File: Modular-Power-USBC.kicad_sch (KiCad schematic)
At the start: 17 parts, among them J1 USB_C_Receptacle_PowerOnly_6P, J2 +12v Rail, J3 -12V Rail, U1 LM66100DCK

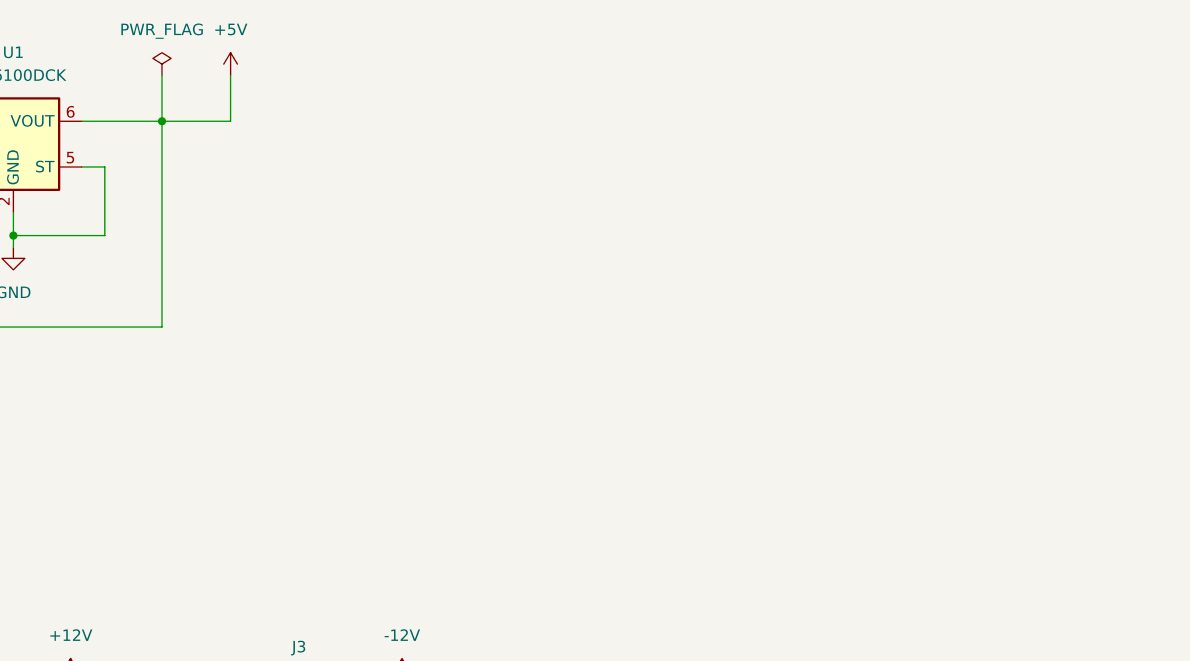
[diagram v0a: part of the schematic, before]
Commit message: Add switch
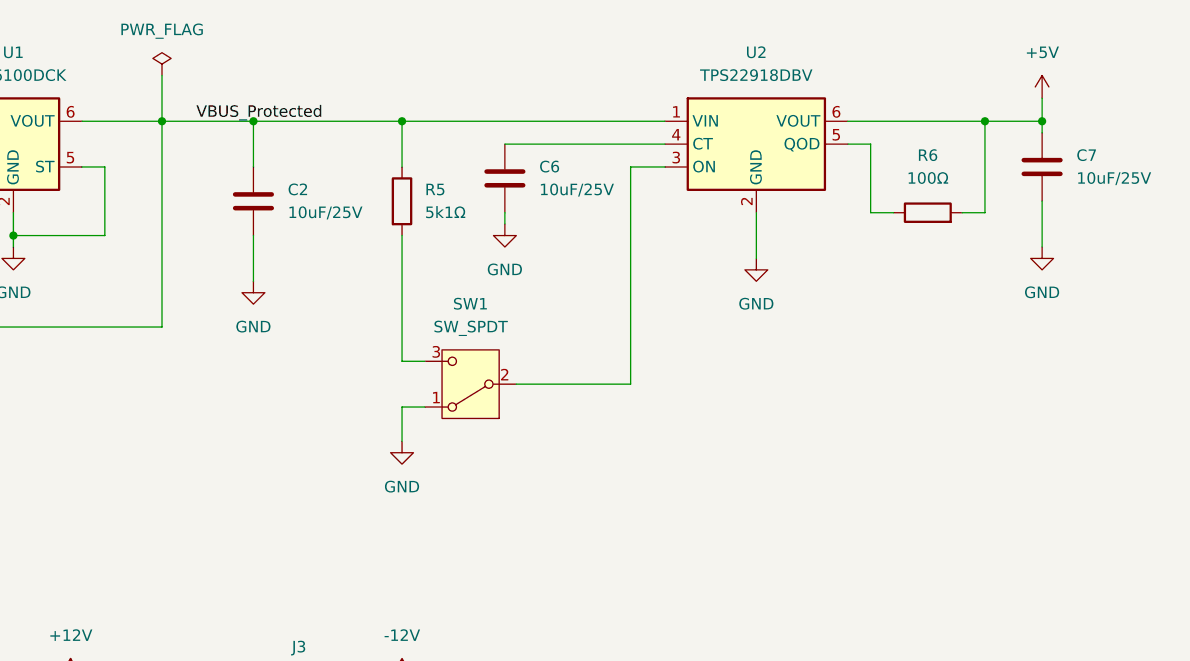
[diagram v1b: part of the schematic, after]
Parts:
- added C2, C6, C7: 10uF/25V, Capacitor_SMD:C_0805_2012Metric_Pad1.18x1.45mm_HandSolder, symbol Device:C
- added R5: 5k1Ω, Resistor_SMD:R_0805_2012Metric_Pad1.20x1.40mm_HandSolder, symbol Device:R
- added R6: 100Ω, Resistor_SMD:R_0805_2012Metric_Pad1.20x1.40mm_HandSolder, symbol Device:R
- added SW1: SW_SPDT, Button_Switch_THT:SW_Slide_SPDT_Straight_CK_OS102011MS2Q, symbol Switch:SW_SPDT
- added U2: TPS22918DBV, Package_TO_SOT_SMD:SOT-23-6, symbol ModularPower:TPS22918DBV
- FB1: footprint (none) -> Modular-Power-USBC:FerriteBead_0805_2012Metric_Pad1.20x1.40mm_HandSolder
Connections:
- net +5V: now also C7.1, R6.2, U2.6 (VOUT); no longer U1.3 (~{CE}), U1.6 (VOUT)
- net GND: now also C2.2, C6.2, C7.2, SW1.1 (A), U2.2 (GND)
- new net: SW1.2 (B), U2.3 (ON)
- new net: R5.2, SW1.3 (C)
- new net: C6.1, U2.4 (CT)
- new net: R6.1, U2.5 (QOD)
- new net VBUS_Protected: C2.1, R5.1, U1.3 (~{CE}), U1.6 (VOUT), U2.1 (VIN)

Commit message: Add README and fixup traces and symbols
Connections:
- net GND: now also J1.SH (SHIELD); no longer J1.S1 (SHIELD)
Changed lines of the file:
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@@
 		(pin "A12"
 		)
-		(pin "S1"
+		(pin "SH"
 		)
 		(instances

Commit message: Drop redundant cap
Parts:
- removed C7: 10uF/25V, Capacitor_SMD:C_0805_2012Metric_Pad1.18x1.45mm_HandSolder, symbol Device:C
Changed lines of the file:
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@@
-	)
-	(junction
-		(at 257.81 43.18)
-		(diameter 0)
-		(color 0 0 0 0)
 	)
 	(junction
@@
 	(wire
 		(pts
-			(xy 257.81 43.18) (xy 257.81 44.45)
-		)
-		(stroke
-			(width 0)
-			(type default)
-		)
-	)
-	(wire
-		(pts
 			(xy 107.95 114.3) (xy 107.95 119.38)
 		)
@@
 	(wire
 		(pts
-			(xy 257.81 52.07) (xy 257.81 57.15)
-		)
-		(stroke
-			(width 0)
-			(type default)
-		)
-	)
-	(wire
-		(pts
 			(xy 198.12 45.72) (xy 215.9 45.72)
 		)
@@
 	(wire
 		(pts
-			(xy 251.46 43.18) (xy 257.81 43.18)
-		)
-		(stroke
-			(width 0)
-			(type default)
-		)
-	)
-	(wire
-		(pts
 			(xy 44.45 120.65) (xy 44.45 118.11)
 		)
@@
 	(wire
 		(pts
-			(xy 257.81 40.64) (xy 257.81 43.18)
+			(xy 251.46 40.64) (xy 251.46 43.18)
 		)
 		(stroke
@@
 	(symbol
 		(lib_id "power:+5V")
-		(at 257.81 40.64 0)
+		(at 251.46 40.64 0)
 		(unit 1)
 		(body_style 1)
@@
 		(fields_autoplaced yes)
 		(property "Reference" "#PWR020"
-			(at 257.81 44.45 0)
+			(at 251.46 44.45 0)
 			(hide yes)
 			(show_name no)
@@
 		)
 		(property "Value" "+5V"
-			(at 257.81 35.56 0)
+			(at 251.46 35.56 0)
 			(show_name no)
 			(do_not_autoplace no)
@@
 		)
 		(property "Footprint" ""
-			(at 257.81 40.64 0)
+			(at 251.46 40.64 0)
 			(hide yes)
 			(show_name no)
@@
 		)
 		(property "Datasheet" ""
-			(at 257.81 40.64 0)
+			(at 251.46 40.64 0)
 			(hide yes)
 			(show_name no)
@@
 		)
 		(property "Description" "Power symbol creates a global label with name \"+5V\""
-			(at 257.81 40.64 0)
+			(at 251.46 40.64 0)
 			(hide yes)
 			(show_name no)
@@
 	)
 	(symbol
-		(lib_id "Device:C")
-		(at 257.81 48.26 0)
-		(unit 1)
-		(body_style 1)
-		(exclude_from_sim no)
-		(in_bom yes)
-		(on_board yes)
-		(in_pos_files yes)
-		(dnp no)
-		(fields_autoplaced yes)
-		(property "Reference" "C7"
-			(at 261.62 46.9899 0)
-			(show_name no)
-			(do_not_autoplace no)
-			(effects
-				(font
-					(size 1.27 1.27)
-				)
-				(justify left)
-			)
-		)
-		(property "Value" "10uF/25V"
-			(at 261.62 49.5299 0)
-			(show_name no)
-			(do_not_autoplace no)
-			(effects
-				(font
-					(size 1.27 1.27)
-				)
-				(justify left)
-			)
-		)
-		(property "Footprint" "Capacitor_SMD:C_0805_2012Metric_Pad1.18x1.45mm_HandSolder"
-			(at 258.7752 52.07 0)
-			(hide yes)
-			(show_name no)
-			(do_not_autoplace no)
-			(effects
-				(font
-					(size 1.27 1.27)
-				)
-			)
-		)
-		(property "Datasheet" ""
-			(at 257.81 48.26 0)
-			(hide yes)
-			(show_name no)
-			(do_not_autoplace no)
-			(effects
-				(font
-					(size 1.27 1.27)
-				)
-			)
-		)
-		(property "Description" "Unpolarized capacitor"
-			(at 257.81 48.26 0)
-			(hide yes)
-			(show_name no)
-			(do_not_autoplace no)
-			(effects
-				(font
-					(size 1.27 1.27)
-				)
-			)
-		)
-		(property "LCSC" "C6119887"
-			(at 257.81 48.26 0)
-			(hide yes)
-			(show_name no)
-			(do_not_autoplace no)
-			(effects
-				(font
-					(size 1.27 1.27)
-				)
-			)
-		)
-		(pin "2"
-		)
-		(pin "1"
-		)
-		(instances
-			(project "Modular-Power-USBC"
-				(path "/f2dd20e6-6351-4f8b-97a2-d33eb2b95f73"
-					(reference "C7")
-					(unit 1)
-				)
-			)
-		)
-	)
-	(symbol
 		(lib_id "Device:R")
 		(at 114.3 157.48 0)
@@
 					(unit 1)
 				)
-			)
-		)
-	)
-	(symbol
-		(lib_id "power:GND")
-		(at 257.81 57.15 0)
-		(unit 1)
-		(body_style 1)
-		(exclude_from_sim no)
-		(in_bom yes)
-		(on_board yes)
-		(in_pos_files yes)
-		(dnp no)
-		(fields_autoplaced yes)
-		(property "Reference" "#PWR019"
-			(at 257.81 63.5 0)
-			(hide yes)
-			(show_name no)
-			(do_not_autoplace no)
-			(effects
-				(font
-					(size 1.27 1.27)
-				)
-			)
-		)
-		(property "Value" "GND"
-			(at 257.81 62.23 0)
-			(show_name no)
-			(do_not_autoplace no)
-			(effects
-				(font
-					(size 1.27 1.27)
-				)
-			)
-		)
-		(property "Footprint" ""
-			(at 257.81 57.15 0)
-			(hide yes)
-			(show_name no)
-			(do_not_autoplace no)
-			(effects
-				(font
-					(size 1.27 1.27)
-				)
-			)
-		)
-		(property "Datasheet" ""
-			(at 257.81 57.15 0)
-			(hide yes)
-			(show_name no)
-			(do_not_autoplace no)
-			(effects
-				(font
-					(size 1.27 1.27)
-				)
-			)
-		)
-		(property "Description" "Power symbol creates a global label with name \"GND\" , ground"
-			(at 257.81 57.15 0)
-			(hide yes)
-			(show_name no)
-			(do_not_autoplace no)
-			(effects
-				(font
-					(size 1.27 1.27)
-				)
-			)
-		)
-		(pin "1"
-		)
-		(instances
-			(project "Modular-Power-USBC"
-				(path "/f2dd20e6-6351-4f8b-97a2-d33eb2b95f73"
-					(reference "#PWR019")
-					(unit 1)
-				)

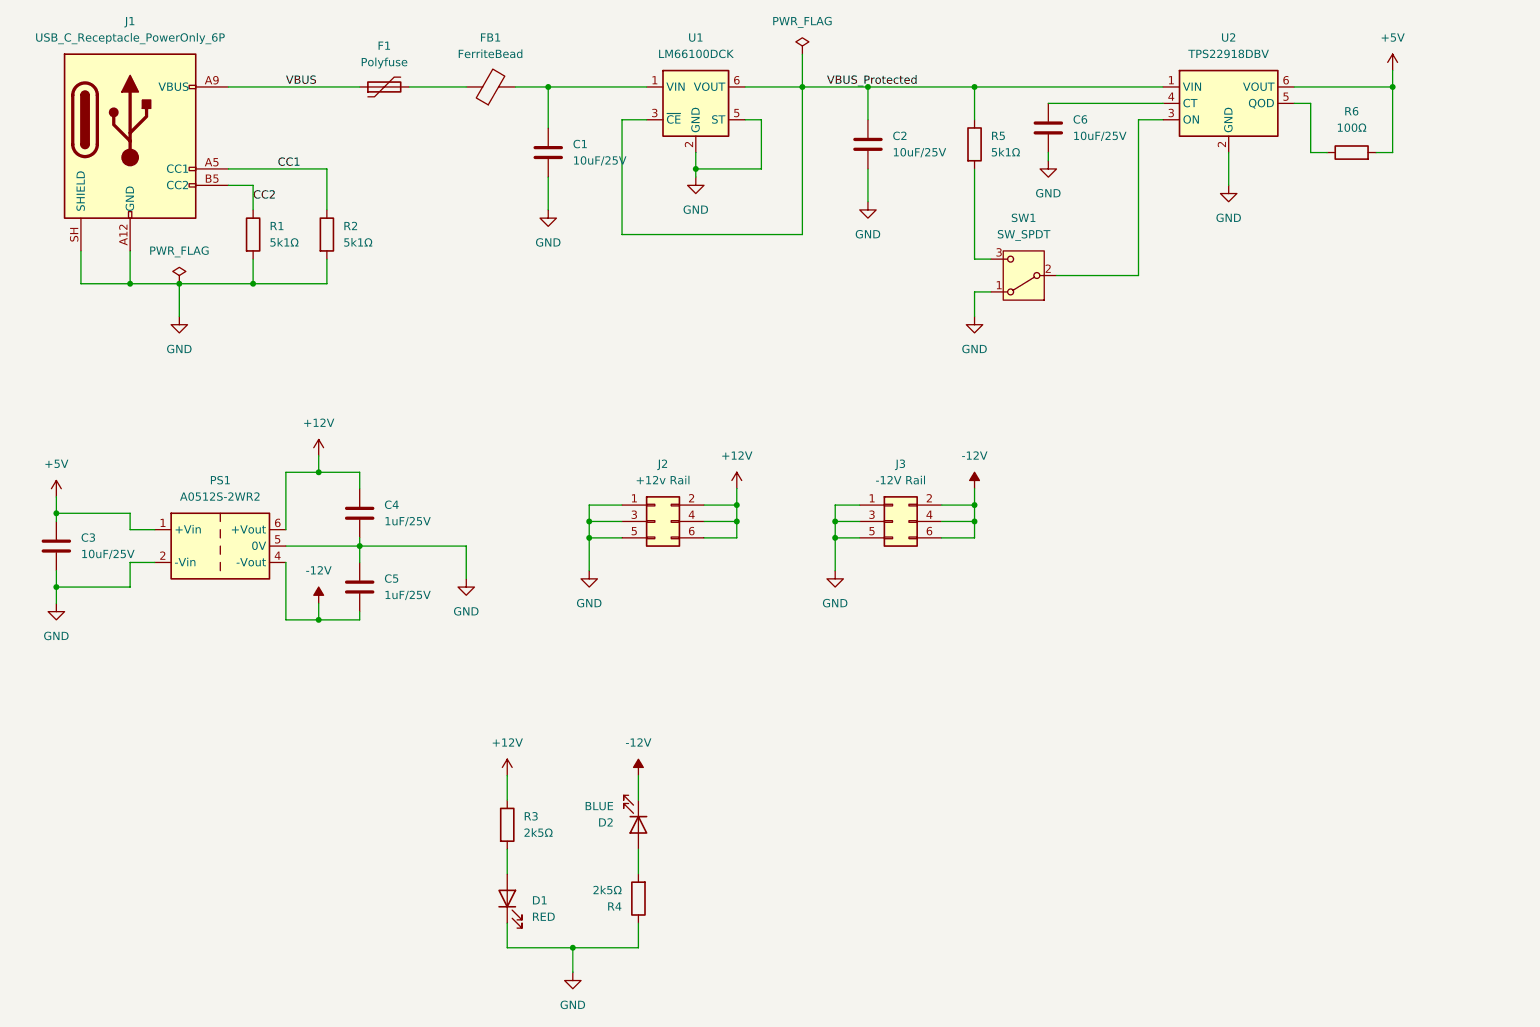
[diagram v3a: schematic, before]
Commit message: Clean up circuit with Gemini's assistance
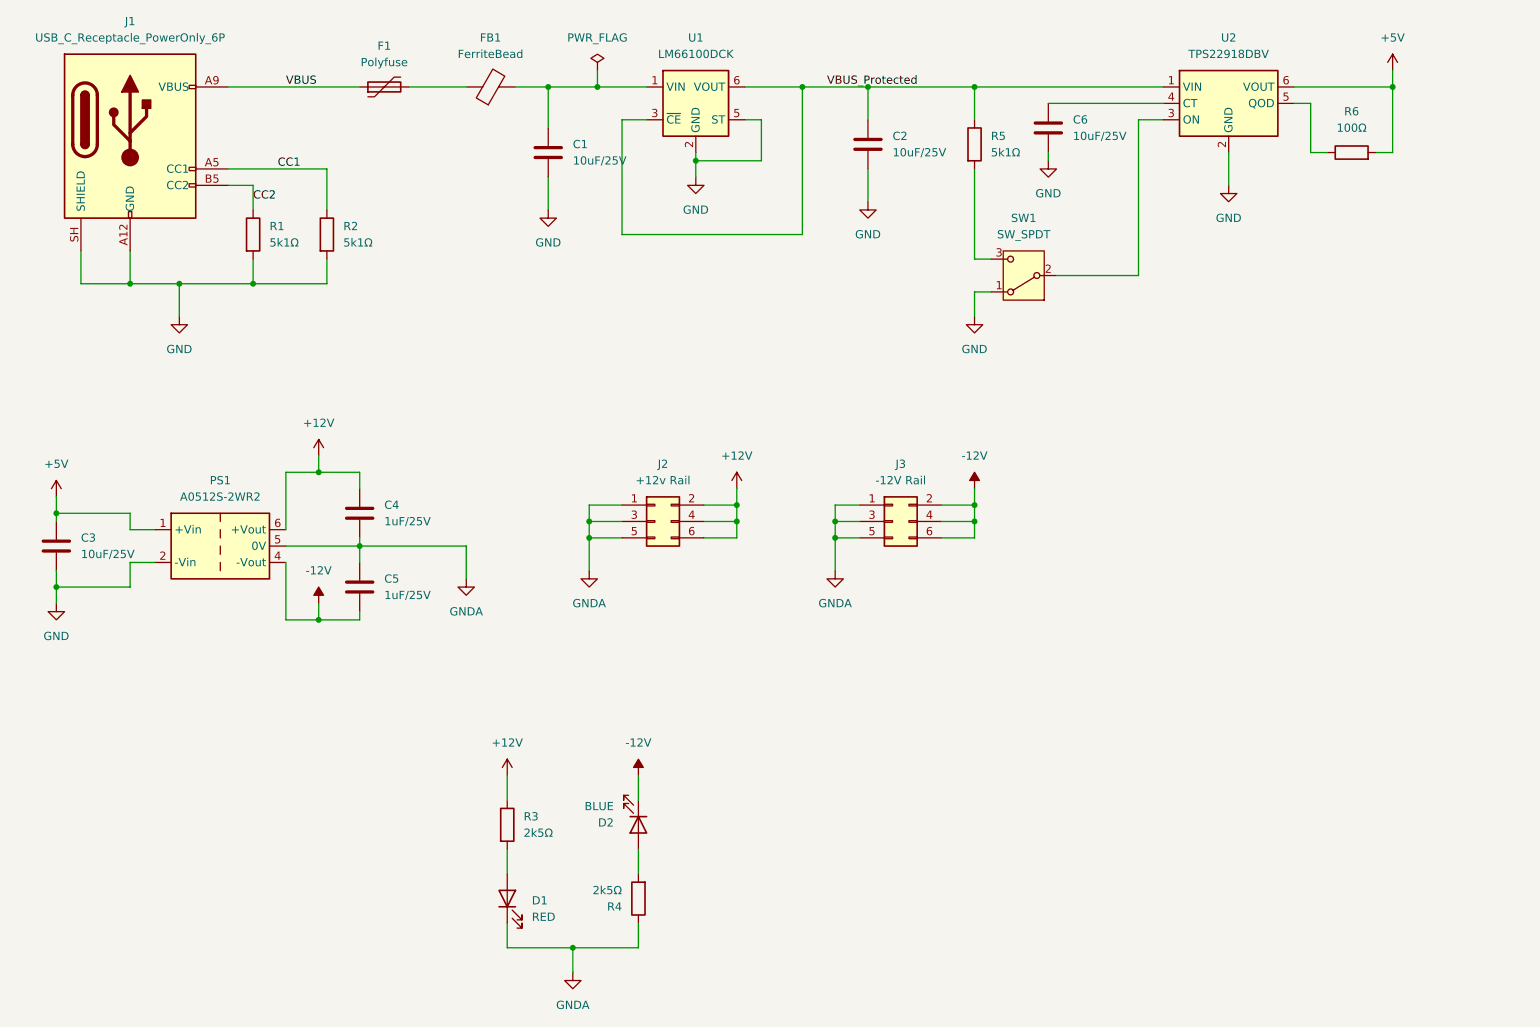
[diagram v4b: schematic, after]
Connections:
- net GND: no longer C4.2, C5.1, D1.1 (K), J2.1 (Pin_1), J2.3 (Pin_3), J2.5 (Pin_5), J3.1 (Pin_1), J3.3 (Pin_3), J3.5 (Pin_5), PS1.5 (0V), R4.1
- new net GNDA: C4.2, C5.1, D1.1 (K), J2.1 (Pin_1), J2.3 (Pin_3), J2.5 (Pin_5), J3.1 (Pin_1), J3.3 (Pin_3), J3.5 (Pin_5), PS1.5 (0V), R4.1

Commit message: Add LCSC part numbers
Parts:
- C4, C5: LCSC (none) -> C116352
- D1: LCSC (none) -> C84256
- D2: LCSC (none) -> C84259
- J2, J3: LCSC (none) -> C7501274
- R3, R4: value 2k5Ω -> 2k2Ω; LCSC (none) -> C2907303
- R6: LCSC (none) -> C2907294
- SW1: LCSC (none) -> C2939725
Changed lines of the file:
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@@
 			)
 		)
+		(property "LCSC" "C2939725"
+			(at 194.31 72.39 0)
+			(hide yes)
+			(show_name no)
+			(do_not_autoplace no)
+			(effects
+				(font
+					(size 1.27 1.27)
+				)
+			)
+		)
 		(pin "2"
 		)
@@
 			)
 		)
+		(property "LCSC" "C116352"
+			(at 91.44 120.65 0)
+			(hide yes)
+			(show_name no)
+			(do_not_autoplace no)
+			(effects
+				(font
+					(size 1.27 1.27)
+				)
+			)
+		)
 		(pin "2"
 		)
@@
 			)
 		)
-		(property "Value" "2k5Ω"
+		(property "Value" "2k2Ω"
 			(at 116.84 158.7499 0)
 			(show_name no)
@@
 			)
 		)
+		(property "LCSC" "C2907303"
+			(at 114.3 157.48 0)
+			(hide yes)
+			(show_name no)
+			(do_not_autoplace no)
+			(effects
+				(font
+					(size 1.27 1.27)
+				)
+			)
+		)
 		(pin "2"
 		)
@@
 			)
 		)
+		(property "LCSC" "C116352"
+			(at 91.44 109.22 0)
+			(hide yes)
+			(show_name no)
+			(do_not_autoplace no)
+			(effects
+				(font
+					(size 1.27 1.27)
+				)
+			)
+		)
 		(pin "2"
 		)
@@
 			)
 		)
+		(property "LCSC" "C7501274"
+			(at 137.16 110.49 0)
+			(hide yes)
+			(show_name no)
+			(do_not_autoplace no)
+			(effects
+				(font
+					(size 1.27 1.27)
+				)
+			)
+		)
 		(pin "1"
 		)
@@
 			)
 		)
+		(property "LCSC" "C84256"
+			(at 114.3 168.91 90)
+			(hide yes)
+			(show_name no)
+			(do_not_autoplace no)
+			(effects
+				(font
+					(size 1.27 1.27)
+				)
+			)
+		)
 		(pin "2"
 		)
@@
 			)
 		)
-		(property "Value" "2k5Ω"
+		(property "Value" "2k2Ω"
 			(at 132.08 167.6401 0)
 			(show_name no)
@@
 			)
 		)
+		(property "LCSC" "C2907303"
+			(at 134.62 168.91 0)
+			(hide yes)
+			(show_name no)
+			(do_not_autoplace no)
+			(effects
+				(font
+					(size 1.27 1.27)
+				)
+			)
+		)
 		(pin "2"
 		)
@@
 			)
 		)
+		(property "LCSC" "C7501274"
+			(at 173.99 110.49 0)
+			(hide yes)
+			(show_name no)
+			(do_not_autoplace no)
+			(effects
+				(font
+					(size 1.27 1.27)
+				)
+			)
+		)
 		(pin "1"
 		)
@@
 			)
 		)
+		(property "LCSC" "C84259"
+			(at 134.62 157.48 90)
+			(hide yes)
+			(show_name no)
+			(do_not_autoplace no)
+			(effects
+				(font
+					(size 1.27 1.27)
+				)
+			)
+		)
 		(pin "2"
 		)
@@
 			(hide yes)
 			(show_name no)
+			(do_not_autoplace no)
+			(effects
+				(font
+					(size 1.27 1.27)
+				)
+			)
+		)
+		(property "LCSC" "C2907294"
+			(at 245.11 53.34 90)
+			(hide yes)
+			(show_name no)

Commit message: Update for production
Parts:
- FB1: LCSC C76818 -> C307778
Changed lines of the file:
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@@
 			)
 		)
-		(property "LCSC" "C76818"
+		(property "LCSC" "C307778"
 			(at 111.76 43.18 90)
 			(hide yes)
